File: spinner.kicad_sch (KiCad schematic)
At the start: 86 parts, among them J1 Micro_SD_Card, SW1 SW_SPDT, U1 AP63205WU, U2 RS0102, U3 SFH617A-3X006, U4 SFH617A-3X006, U5 SFH617A-3X006

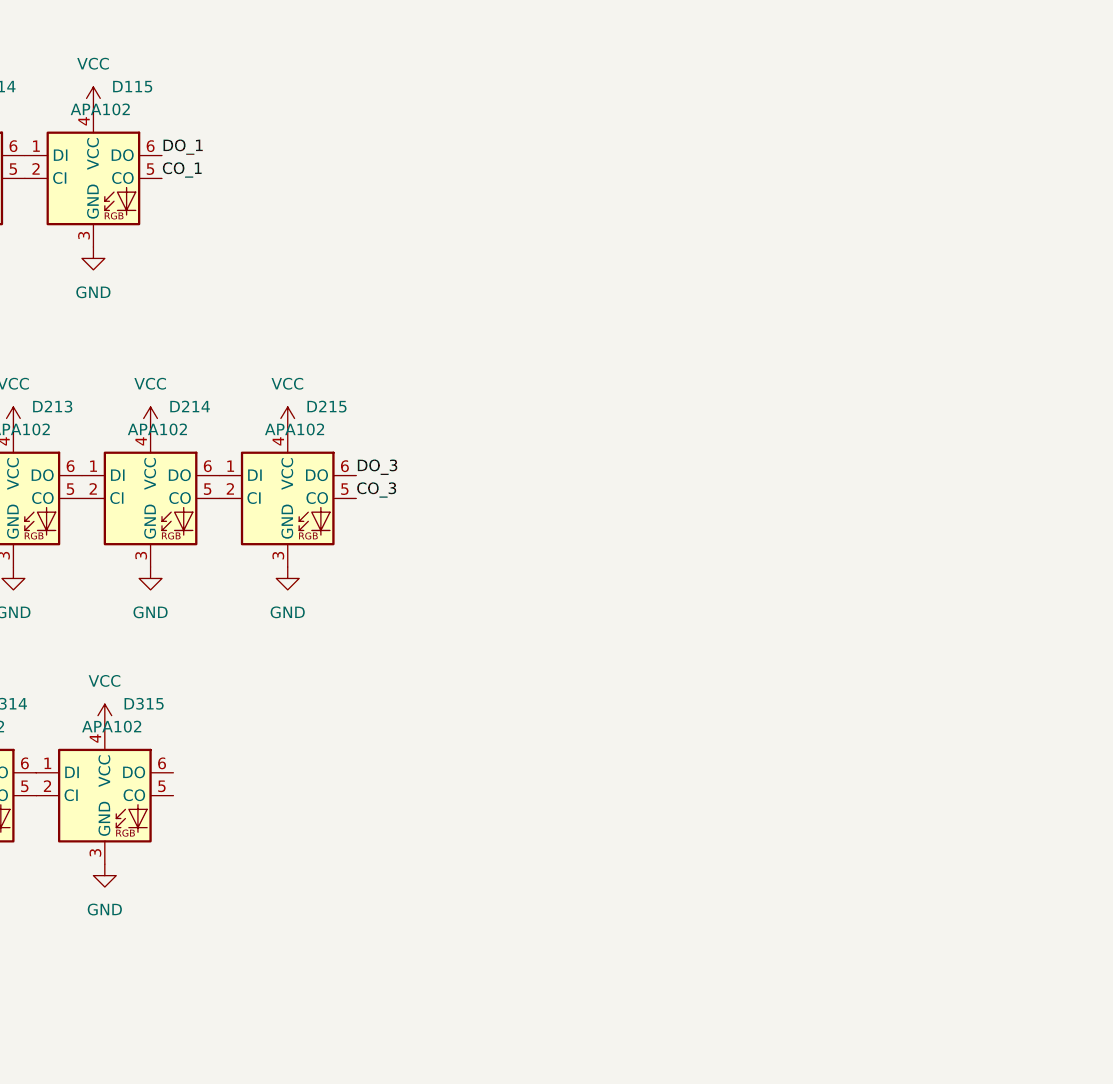
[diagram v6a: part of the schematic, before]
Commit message: Place more LEDs.  Not quite done.
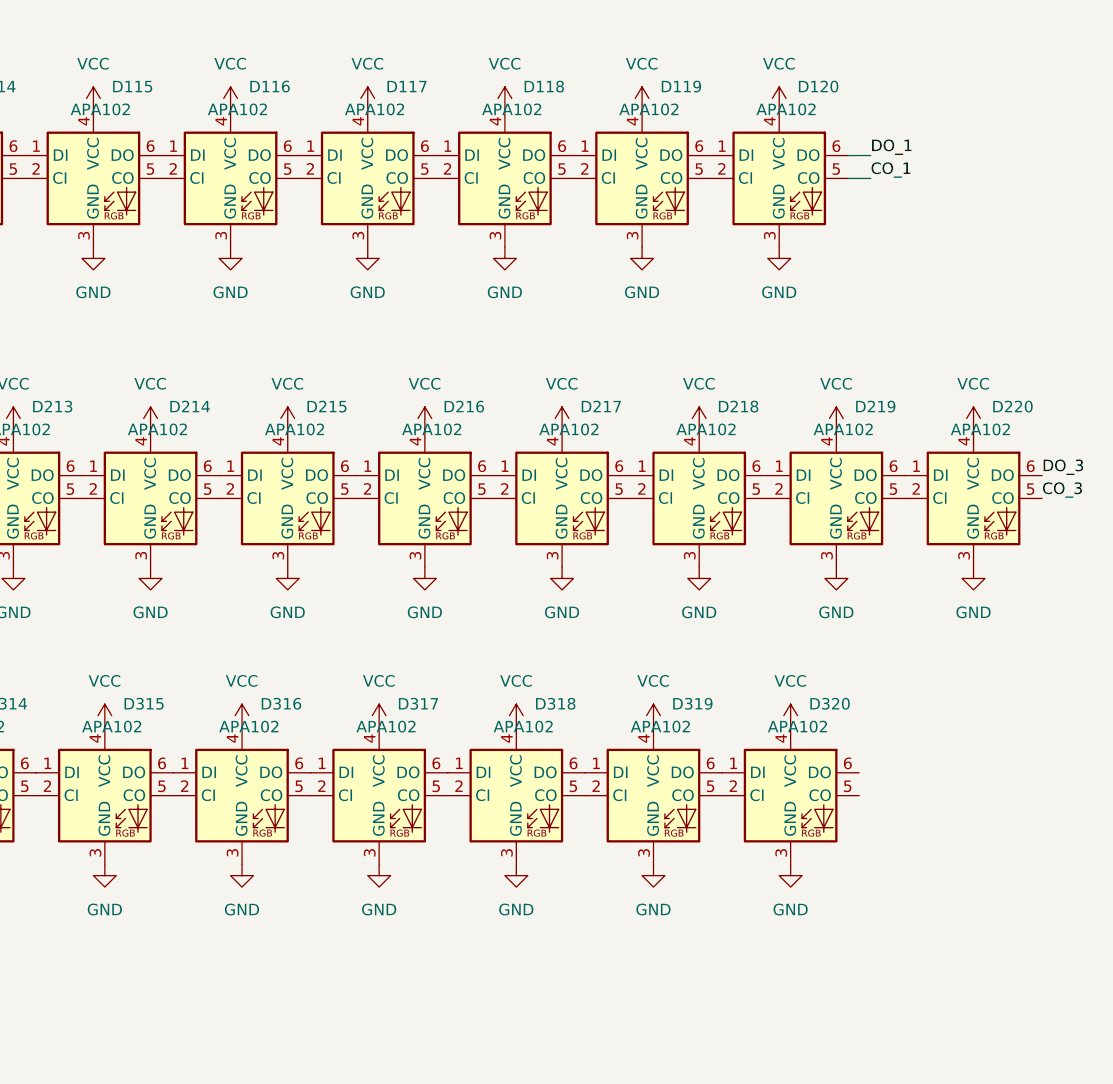
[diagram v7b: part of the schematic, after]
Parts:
- added D116, D117, D118, D119, D120, D216, D217, D218, D219, D220, D316, D317, D318, D319, D320: APA102, Library:SK9822-hakz, symbol LED:APA102
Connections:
- net CO_1: now also D120.5 (CO); no longer D115.5 (CO)
- net CO_3: now also D220.5 (CO); no longer D215.5 (CO)
- net DO_1: now also D120.6 (DO); no longer D115.6 (DO)
- net DO_3: now also D220.6 (DO); no longer D215.6 (DO)
- net GND: now also D116.3 (GND), D117.3 (GND), D118.3 (GND), D119.3 (GND), D120.3 (GND), D216.3 (GND), D217.3 (GND), D218.3 (GND), D219.3 (GND), D220.3 (GND), D316.3 (GND), D317.3 (GND), D318.3 (GND), D319.3 (GND), D320.3 (GND)
- net VCC: now also D116.4 (VCC), D117.4 (VCC), D118.4 (VCC), D119.4 (VCC), D120.4 (VCC), D216.4 (VCC), D217.4 (VCC), D218.4 (VCC), D219.4 (VCC), D220.4 (VCC), D316.4 (VCC), D317.4 (VCC), D318.4 (VCC), D319.4 (VCC), D320.4 (VCC)
- net at D315.5 (CO): now also D316.2 (CI)
- net at D315.6 (DO): now also D316.1 (DI)
- new net: D319.6 (DO), D320.1 (DI)
- new net: D319.5 (CO), D320.2 (CI)
- new net: D218.6 (DO), D219.1 (DI)
- new net: D218.5 (CO), D219.2 (CI)
- new net: D219.5 (CO), D220.2 (CI)
- new net: D219.6 (DO), D220.1 (DI)
- new net: D117.6 (DO), D118.1 (DI)
- new net: D117.5 (CO), D118.2 (CI)
- new net: D118.5 (CO), D119.2 (CI)
- new net: D118.6 (DO), D119.1 (DI)
- new net: D215.5 (CO), D216.2 (CI)
- new net: D215.6 (DO), D216.1 (DI)
- new net: D317.6 (DO), D318.1 (DI)
- new net: D317.5 (CO), D318.2 (CI)
- new net: D318.5 (CO), D319.2 (CI)
- new net: D318.6 (DO), D319.1 (DI)
- new net: D119.6 (DO), D120.1 (DI)
- new net: D119.5 (CO), D120.2 (CI)
- new net: D216.6 (DO), D217.1 (DI)
- new net: D216.5 (CO), D217.2 (CI)
- new net: D217.5 (CO), D218.2 (CI)
- new net: D217.6 (DO), D218.1 (DI)
- new net: D115.6 (DO), D116.1 (DI)
- new net: D115.5 (CO), D116.2 (CI)
- new net: D116.5 (CO), D117.2 (CI)
- new net: D116.6 (DO), D117.1 (DI)
- new net: D316.5 (CO), D317.2 (CI)
- new net: D316.6 (DO), D317.1 (DI)

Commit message: IDK.  Adding lib things.  Need to update kicad.
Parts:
- removed A1: Adafruit_HUZZAH_ESP8266_breakout, Library:huzz_hakz, symbol MCU_Module:Adafruit_HUZZAH_ESP8266_breakout
- added ?: ESP32-S3-WROOM-1, symbol hakz2:ESP32-S3-WROOM-1
- added D121, D122, D123, D124, D221, D222, D223, D224, D321, D322, D323, D324: APA102, Library:SK9822-hakz, symbol LED:APA102
- added U6: ESP32-WROVER, Library:ESP32-WROVER, symbol hakz:ESP32-WROVER
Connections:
- net CO_1: now also D124.5 (CO); no longer D120.5 (CO)
- net CO_3: now also D224.5 (CO); no longer D220.5 (CO)
- net DO_1: now also D124.6 (DO); no longer D120.6 (DO)
- net DO_3: now also D224.6 (DO); no longer D220.6 (DO)
- net GND: now also D121.3 (GND), D122.3 (GND), D123.3 (GND), D124.3 (GND), D221.3 (GND), D222.3 (GND), D223.3 (GND), D224.3 (GND), D321.3 (GND), D322.3 (GND), D323.3 (GND), D324.3 (GND)
- net VCC: now also D121.4 (VCC), D122.4 (VCC), D123.4 (VCC), D124.4 (VCC), D221.4 (VCC), D222.4 (VCC), D223.4 (VCC), D224.4 (VCC), D321.4 (VCC), D322.4 (VCC), D323.4 (VCC), D324.4 (VCC)
- net at D320.5 (CO): now also D321.2 (CI)
- net at D320.6 (DO): now also D321.1 (DI)
- new net: D321.5 (CO), D322.2 (CI)
- new net: D321.6 (DO), D322.1 (DI)
- new net: D122.6 (DO), D123.1 (DI)
- new net: D122.5 (CO), D123.2 (CI)
- new net: D123.5 (CO), D124.2 (CI)
- new net: D123.6 (DO), D124.1 (DI)
- new net: D220.6 (DO), D221.1 (DI)
- new net: D220.5 (CO), D221.2 (CI)
- new net: D221.5 (CO), D222.2 (CI)
- new net: D221.6 (DO), D222.1 (DI)
- new net: D120.5 (CO), D121.2 (CI)
- new net: D120.6 (DO), D121.1 (DI)
- new net: D322.6 (DO), D323.1 (DI)
- new net: D322.5 (CO), D323.2 (CI)
- new net: D323.5 (CO), D324.2 (CI)
- new net: D323.6 (DO), D324.1 (DI)
- new net: D121.6 (DO), D122.1 (DI)
- new net: D121.5 (CO), D122.2 (CI)
- new net: D222.5 (CO), D223.2 (CI)
- new net: D222.6 (DO), D223.1 (DI)
- new net: ?.1 (GND), ?.40 (GND), ?.41 (GND)
- new net: D223.5 (CO), D224.2 (CI)
- new net: D223.6 (DO), D224.1 (DI)
